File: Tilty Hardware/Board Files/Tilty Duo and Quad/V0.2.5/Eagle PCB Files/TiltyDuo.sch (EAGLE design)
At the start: 50 parts, among them U1 TEENSY_3.0_OUTER-PINS28-DIP_S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, U2 HC-09_BREAKOUT, U3 MPL3115A2LGA8, U4 LM2931, U5 MPU-6050, U6 HMC5883LSMD, U7 SPI_FLASH-X25XXSMD

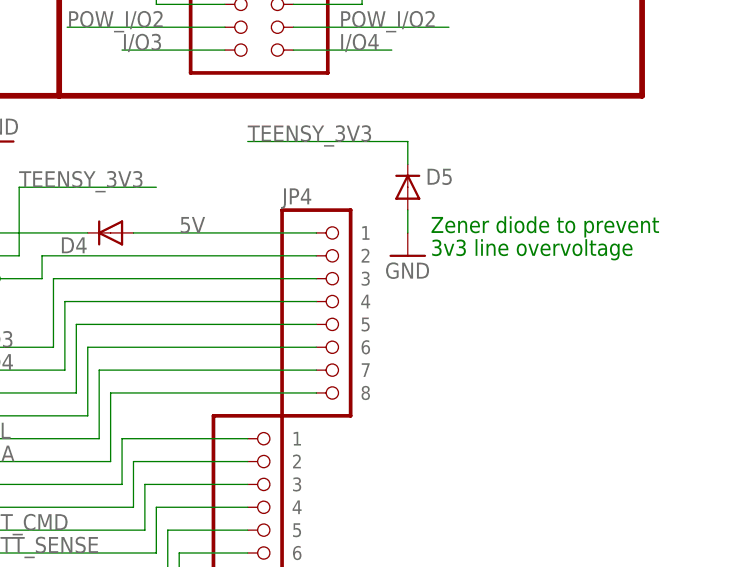
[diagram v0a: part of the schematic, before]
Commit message: Minor changes
Added current limit resistor to zener shunt on Tilty Duo/Quad.
Added power supply solder jumper to Advanced IMU altimeter.
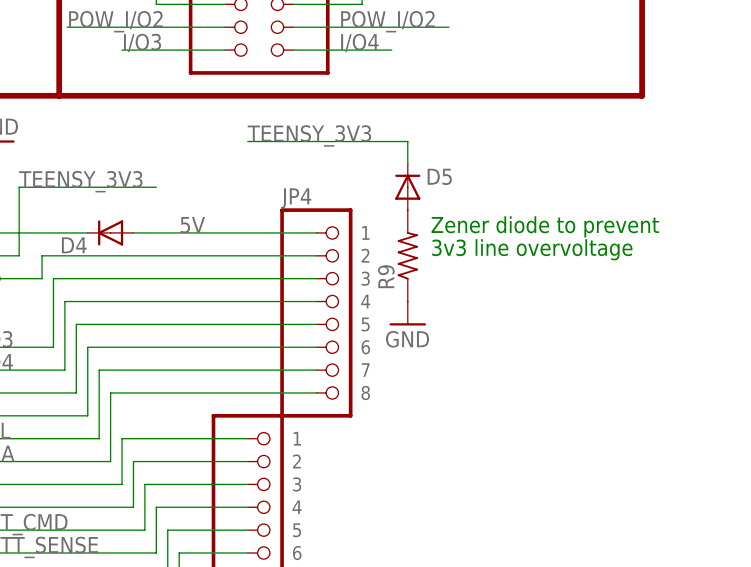
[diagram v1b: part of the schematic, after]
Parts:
- added R9: (no value), resistor:R-US_R0603
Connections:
- new net N$22: D5.A, R9.2
- net GND: now also R9.1; no longer D5.A
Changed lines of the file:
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@@
 <part name="SJ5" library="SparkFun-Passives" deviceset="SOLDERJUMPER" device="TRACE"/>
 <part name="SJ7" library="SparkFun-Passives" deviceset="SOLDERJUMPER" device="TRACE"/>
+<part name="R9" library="resistor" deviceset="R-US_" device="R0603"/>
 </parts>
 <sheets>
@@
 <attribute name="PART#" x="251.46" y="66.04" size="1.778" layer="96" rot="R90" display="off"/>
 </instance>
-<instance part="GND23" gate="1" x="251.46" y="58.42"/>
+<instance part="GND23" gate="1" x="251.46" y="50.8"/>
 <instance part="JP4" gate="G$1" x="241.3" y="53.34" smashed="yes">
 <attribute name="NAME" x="237.49" y="64.135" size="1.778" layer="95"/>
@@
 <attribute name="NAME" x="88.9" y="172.72" size="1.778" layer="95" rot="R180"/>
 </instance>
+<instance part="R9" gate="G$1" x="251.46" y="58.42" rot="R90"/>
 </instances>
 <busses>
@@
 </segment>
 <segment>
-<pinref part="D5" gate="G$1" pin="A"/>
-<pinref part="GND23" gate="1" pin="GND"/>
-<wire x1="251.46" y1="60.96" x2="251.46" y2="63.5" width="0.1524" layer="91"/>
-</segment>
-<segment>
 <pinref part="C6" gate="G$1" pin="2"/>
 <pinref part="GND15" gate="1" pin="GND"/>
 <wire x1="78.74" y1="167.64" x2="83.82" y2="167.64" width="0.1524" layer="91"/>
+</segment>
+<segment>
+<pinref part="R9" gate="G$1" pin="1"/>
+<pinref part="GND23" gate="1" pin="GND"/>
 </segment>
 </net>
@@
 </segment>
 </net>
+<net name="N$22" class="0">
+<segment>
+<pinref part="D5" gate="G$1" pin="A"/>
+<pinref part="R9" gate="G$1" pin="2"/>
+</segment>
+</net>

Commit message: Lots of little updates!
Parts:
- removed D4: (no value), SparkFun-DiscreteSemi:DIODESOT23
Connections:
- removed net N$15: D4.C, U1.VIN
- net 5V: now also U1.VIN; no longer D4.A
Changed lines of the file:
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@@
 <part name="R4" library="resistor" deviceset="R-US_" device="R0603" value="68"/>
 <part name="SJ4" library="SparkFun-Passives" deviceset="SOLDERJUMPER" device="TRACE"/>
-<part name="D4" library="SparkFun-DiscreteSemi" deviceset="DIODE" device="SOT23">
-<attribute name="PART#" value="BAT54FSTR-ND"/>
-</part>
 <part name="D5" library="SparkFun-DiscreteSemi" deviceset="DIODE" device="SOT23">
 <attribute name="PART#" value="BZX84C3V3LT1GOSCT-ND"/>
@@
 <attribute name="NAME" x="105.41" y="71.12" size="1.778" layer="95"/>
 </instance>
-<instance part="D4" gate="G$1" x="218.44" y="60.96" rot="R180">
-<attribute name="PART#" x="218.44" y="60.96" size="1.778" layer="96" rot="R180" display="off"/>
-</instance>
 <instance part="D5" gate="G$1" x="251.46" y="66.04" smashed="yes" rot="R90">
 <attribute name="NAME" x="256.54" y="68.0974" size="1.778" layer="95" rot="R180"/>
@@
 </segment>
 <segment>
-<pinref part="D4" gate="G$1" pin="A"/>
-<wire x1="220.98" y1="60.96" x2="241.3" y2="60.96" width="0.1524" layer="91"/>
+<wire x1="203.2" y1="60.96" x2="241.3" y2="60.96" width="0.1524" layer="91"/>
 <label x="226.06" y="60.96" size="1.778" layer="95"/>
 <pinref part="JP4" gate="G$1" pin="1"/>
+<pinref part="U1" gate="G$1" pin="VIN"/>
 </segment>
 </net>
@@
 </segment>
 </net>
-<net name="N$15" class="0">
-<segment>
-<pinref part="D4" gate="G$1" pin="C"/>
-<pinref part="U1" gate="G$1" pin="VIN"/>
-<wire x1="215.9" y1="60.96" x2="203.2" y2="60.96" width="0.1524" layer="91"/>
-</segment>
-</net>

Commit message: Lots of little changes
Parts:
- U2: value HC-09_BREAKOUT -> MPU-6050; device csr:HC-09_BREAKOUT -> SparkFun-Sensors:MPU-6050
- U3: value MPL3115A2LGA8 -> LM2931; device SparkFun-Sensors:MPL3115A2LGA8 -> on-semiconductor:LM2931; COST (none) -> 0.53
- U4: value LM2931 -> SPI_FLASH-X25XXSMD; device on-semiconductor:LM2931 -> SparkFun-DigitalIC:SPI_FLASH-X25XXSMD; COST 0.53 -> (none); PART# (none) -> S25FL204K0TMFI043
- U5: value MPU-6050 -> HC-09_BREAKOUT; device SparkFun-Sensors:MPU-6050 -> csr:HC-09_BREAKOUT
- U7: value SPI_FLASH-X25XXSMD -> MPL3115A2LGA8; device SparkFun-DigitalIC:SPI_FLASH-X25XXSMD -> SparkFun-Sensors:MPL3115A2LGA8; PART# S25FL204K0TMFI043 -> (none)
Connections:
- net 5V: now also U3.5V; no longer U4.5V
- net AUXCL: now also U2.AUXCL; no longer U5.AUXCL
- net AUXDA: now also U2.AUXDA; no longer U5.AUXDA
- net CMD: now also U5.PIO11; no longer U2.PIO11
- net CS: now also U4.CS; no longer U7.CS
- net GND: now also U2.AD0, U2.CLKIN, U2.FSYNC, U5.GND2, U5.GND3; no longer U2.GND2, U2.GND3, U5.AD0, U5.CLKIN, U5.FSYNC
- net MISO: now also U4.MISO; no longer U7.MISO
- net MOSI: now also U4.MOSI; no longer U7.MOSI
- net N$1: now also U2.REGOUT; no longer U5.REGOUT
- net N$14: now also U5.PIO8; no longer U2.PIO8
- net N$16: now also U2.INT; no longer U5.INT
- net N$2: now also U2.CPOUT; no longer U5.CPOUT
- net N$21: now also U7.CAP; no longer U3.CAP
- net RX1: now also U5.UART_TX; no longer U2.UART_TX
- net SCK: now also U4.SCK; no longer U7.SCK
- net SCL: now also U2.SCL, U7.SCL; no longer U3.SCL, U5.SCL
- net SDA: now also U2.SDA, U7.SDA; no longer U3.SDA, U5.SDA
- net TEENSY_3V3: now also U2.VDD, U2.V_LOGIC, U4.HOLD, U4.VCC, U4.WP, U5.RESET, U5.VCC, U7.VDD, U7.VDDIO; no longer U2.RESET, U2.VCC, U3.VDD, U3.VDDIO, U5.VDD, U5.V_LOGIC, U7.HOLD, U7.VCC, U7.WP
- net TX1: now also U5.UART_RX; no longer U2.UART_RX
- net VBATT: now also U3.VIN; no longer U4.VIN
- net YEL_LED: now also U5.PIO9; no longer U2.PIO9
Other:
- moved on the sheet: U7
